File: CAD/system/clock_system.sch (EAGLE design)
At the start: 14 parts

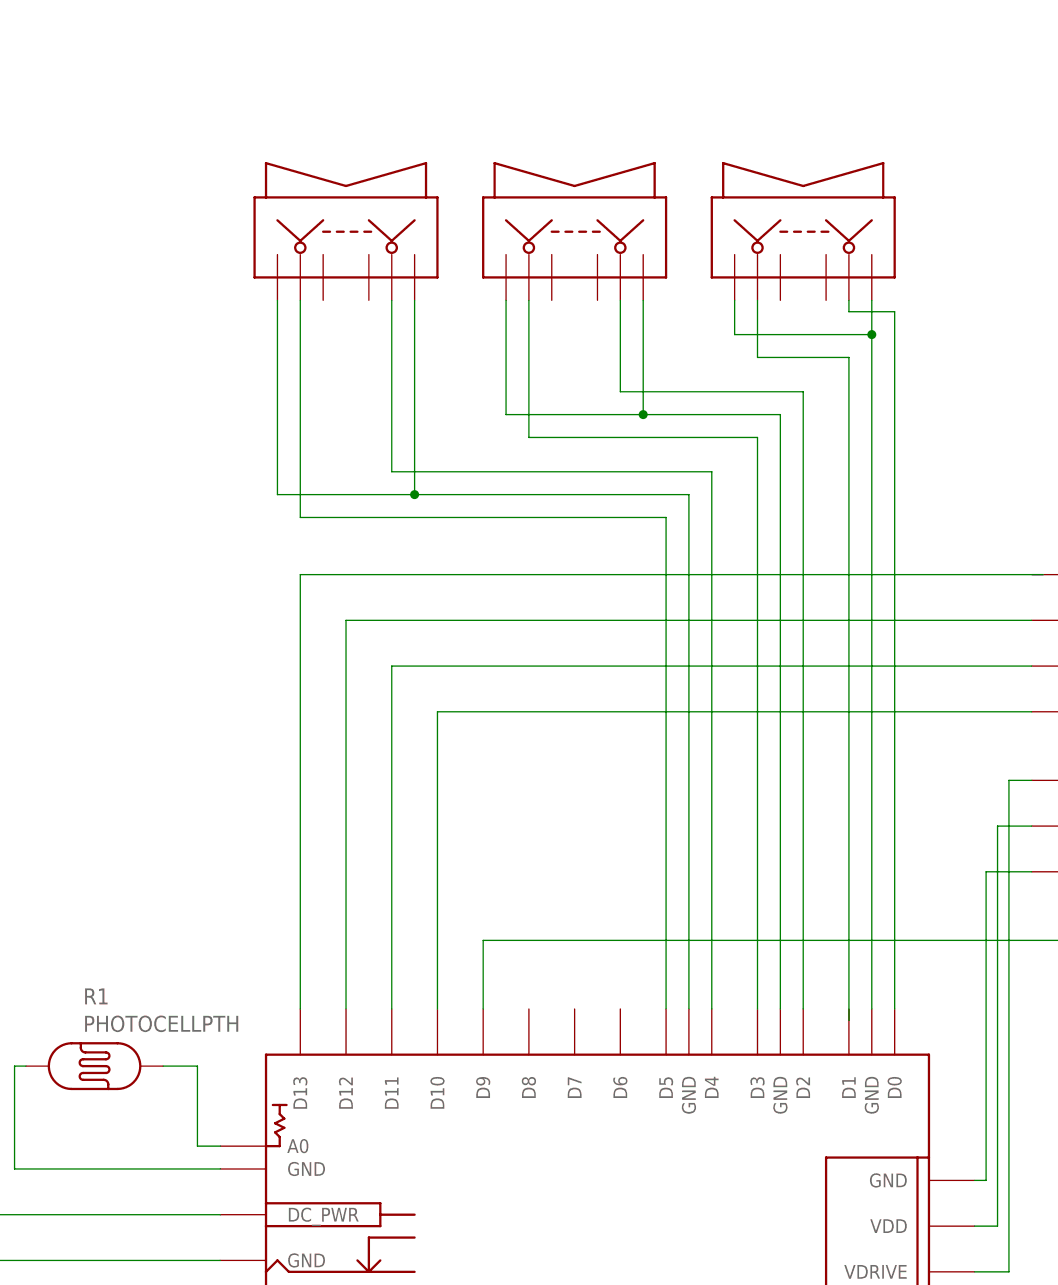
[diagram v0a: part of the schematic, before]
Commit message: Started refactoring code to use new class
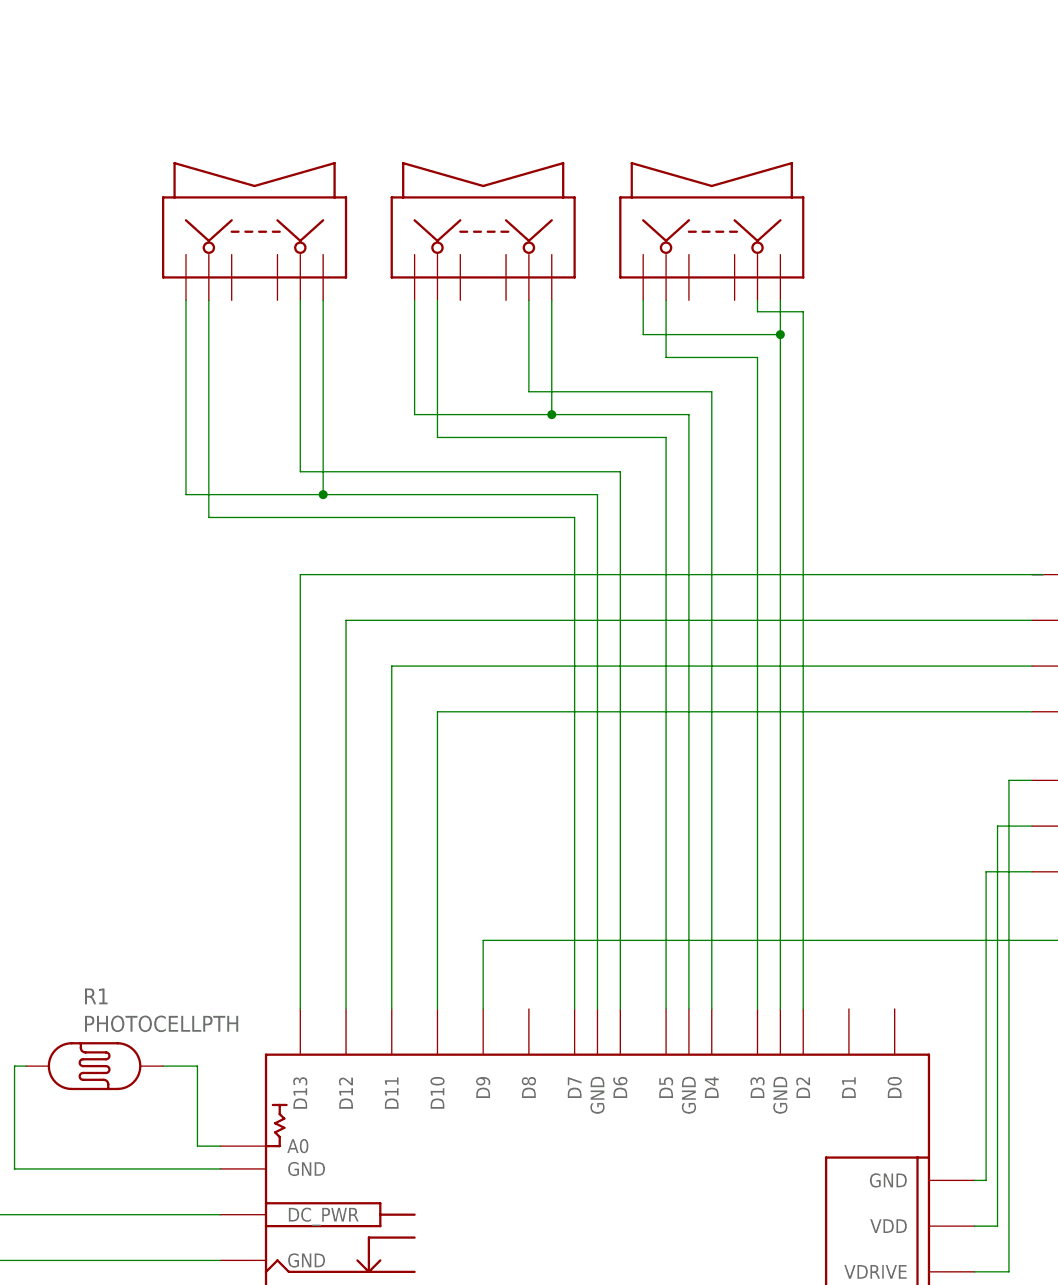
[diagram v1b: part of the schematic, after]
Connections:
- net N$62: now also MOBO.D6; no longer MOBO.D4
- net N$63: now also MOBO.D5; no longer MOBO.D3
- net N$64: now also MOBO.D2; no longer MOBO.D0
- net N$65: now also MOBO.D3
- net N$67: now also MOBO.D4; no longer MOBO.D2
- net N$68: now also MOBO.D7; no longer MOBO.D5
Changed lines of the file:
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@@
 <instance part="MIN2" gate="G$1" x="370.84" y="124.46"/>
 <instance part="COLON" gate="G$1" x="255.27" y="124.46"/>
-<instance part="U$3" gate="G$1" x="81.28" y="124.46" rot="R90"/>
-<instance part="U$1" gate="G$1" x="55.88" y="124.46" rot="R90"/>
-<instance part="U$2" gate="G$1" x="30.48" y="124.46" rot="R90"/>
+<instance part="U$3" gate="G$1" x="71.12" y="124.46" rot="R90"/>
+<instance part="U$1" gate="G$1" x="45.72" y="124.46" rot="R90"/>
+<instance part="U$2" gate="G$1" x="20.32" y="124.46" rot="R90"/>
 <instance part="R1" gate="G$1" x="2.54" y="31.75" smashed="yes">
 <attribute name="NAME" x="1.27" y="38.608" size="1.778" layer="95"/>
@@
 <segment>
 <pinref part="U$1" gate="G$1" pin="P$2"/>
-<wire x1="50.8" y1="116.84" x2="50.8" y2="101.6" width="0.1524" layer="91"/>
-<wire x1="50.8" y1="101.6" x2="76.2" y2="101.6" width="0.1524" layer="91"/>
+<wire x1="40.64" y1="116.84" x2="40.64" y2="101.6" width="0.1524" layer="91"/>
+<wire x1="40.64" y1="101.6" x2="66.04" y2="101.6" width="0.1524" layer="91"/>
+<pinref part="MOBO" gate="G$1" pin="D5"/>
+<wire x1="66.04" y1="38.1" x2="66.04" y2="101.6" width="0.1524" layer="91"/>
+</segment>
+</net>
+<net name="N$66" class="0">
+<segment>
+<pinref part="U$1" gate="G$1" pin="P$1"/>
+<wire x1="38.1" y1="116.84" x2="38.1" y2="104.14" width="0.1524" layer="91"/>
+<pinref part="U$1" gate="G$1" pin="P$6"/>
+<wire x1="38.1" y1="104.14" x2="53.34" y2="104.14" width="0.1524" layer="91"/>
+<wire x1="53.34" y1="104.14" x2="53.34" y2="116.84" width="0.1524" layer="91"/>
+<wire x1="68.58" y1="104.14" x2="53.34" y2="104.14" width="0.1524" layer="91"/>
+<junction x="53.34" y="104.14"/>
+<pinref part="MOBO" gate="G$1" pin="GND@3"/>
+<wire x1="68.58" y1="104.14" x2="68.58" y2="38.1" width="0.1524" layer="91"/>
+</segment>
+</net>
+<net name="N$67" class="0">
+<segment>
+<pinref part="U$1" gate="G$1" pin="P$5"/>
+<wire x1="71.12" y1="106.68" x2="50.8" y2="106.68" width="0.1524" layer="91"/>
+<wire x1="50.8" y1="106.68" x2="50.8" y2="116.84" width="0.1524" layer="91"/>
+<pinref part="MOBO" gate="G$1" pin="D4"/>
+<wire x1="71.12" y1="38.1" x2="71.12" y2="106.68" width="0.1524" layer="91"/>
+</segment>
+</net>
+<net name="N$61" class="0">
+<segment>
+<pinref part="U$3" gate="G$1" pin="P$6"/>
+<wire x1="78.74" y1="116.84" x2="78.74" y2="113.03" width="0.1524" layer="91"/>
+<pinref part="U$3" gate="G$1" pin="P$1"/>
+<wire x1="63.5" y1="116.84" x2="63.5" y2="113.03" width="0.1524" layer="91"/>
+<wire x1="63.5" y1="113.03" x2="78.74" y2="113.03" width="0.1524" layer="91"/>
+<pinref part="MOBO" gate="G$1" pin="GND@2"/>
+<wire x1="78.74" y1="113.03" x2="78.74" y2="38.1" width="0.1524" layer="91"/>
+<junction x="78.74" y="113.03"/>
+</segment>
+</net>
+<net name="N$64" class="0">
+<segment>
+<pinref part="U$3" gate="G$1" pin="P$5"/>
+<wire x1="76.2" y1="116.84" x2="76.2" y2="115.57" width="0.1524" layer="91"/>
+<wire x1="76.2" y1="115.57" x2="81.28" y2="115.57" width="0.1524" layer="91"/>
+<pinref part="MOBO" gate="G$1" pin="D2"/>
+<wire x1="81.28" y1="115.57" x2="81.28" y2="38.1" width="0.1524" layer="91"/>
+</segment>
+</net>
+<net name="N$65" class="0">
+<segment>
+<pinref part="U$3" gate="G$1" pin="P$2"/>
+<wire x1="66.04" y1="116.84" x2="66.04" y2="110.49" width="0.1524" layer="91"/>
+<wire x1="66.04" y1="110.49" x2="76.2" y2="110.49" width="0.1524" layer="91"/>
 <pinref part="MOBO" gate="G$1" pin="D3"/>
-<wire x1="76.2" y1="101.6" x2="76.2" y2="38.1" width="0.1524" layer="91"/>
-</segment>
-</net>
-<net name="N$66" class="0">
-<segment>
-<pinref part="U$1" gate="G$1" pin="P$1"/>
-<wire x1="48.26" y1="116.84" x2="48.26" y2="104.14" width="0.1524" layer="91"/>
-<pinref part="U$1" gate="G$1" pin="P$6"/>
-<wire x1="48.26" y1="104.14" x2="63.5" y2="104.14" width="0.1524" layer="91"/>
-<wire x1="63.5" y1="104.14" x2="63.5" y2="116.84" width="0.1524" layer="91"/>
-<wire x1="78.74" y1="104.14" x2="63.5" y2="104.14" width="0.1524" layer="91"/>
-<junction x="63.5" y="104.14"/>
-<pinref part="MOBO" gate="G$1" pin="GND@3"/>
-<wire x1="78.74" y1="104.14" x2="78.74" y2="38.1" width="0.1524" layer="91"/>
-</segment>
-</net>
-<net name="N$67" class="0">
-<segment>
-<pinref part="U$1" gate="G$1" pin="P$5"/>
-<wire x1="81.28" y1="106.68" x2="60.96" y2="106.68" width="0.1524" layer="91"/>
-<wire x1="60.96" y1="106.68" x2="60.96" y2="116.84" width="0.1524" layer="91"/>
-<pinref part="MOBO" gate="G$1" pin="D2"/>
-<wire x1="81.28" y1="106.68" x2="81.28" y2="38.1" width="0.1524" layer="91"/>
-</segment>
-</net>
-<net name="N$61" class="0">
-<segment>
-<pinref part="U$3" gate="G$1" pin="P$6"/>
-<pinref part="MOBO" gate="G$1" pin="GND@2"/>
-<wire x1="88.9" y1="116.84" x2="88.9" y2="113.03" width="0.1524" layer="91"/>
-<pinref part="U$3" gate="G$1" pin="P$1"/>
-<wire x1="88.9" y1="113.03" x2="88.9" y2="38.1" width="0.1524" layer="91"/>
-<wire x1="73.66" y1="116.84" x2="73.66" y2="113.03" width="0.1524" layer="91"/>
-<wire x1="73.66" y1="113.03" x2="88.9" y2="113.03" width="0.1524" layer="91"/>
-<junction x="88.9" y="113.03"/>
-</segment>
-</net>
-<net name="N$64" class="0">
-<segment>
-<pinref part="U$3" gate="G$1" pin="P$5"/>
-<wire x1="86.36" y1="116.84" x2="86.36" y2="115.57" width="0.1524" layer="91"/>
-<pinref part="MOBO" gate="G$1" pin="D0"/>
-<wire x1="86.36" y1="115.57" x2="91.44" y2="115.57" width="0.1524" layer="91"/>
-<wire x1="91.44" y1="115.57" x2="91.44" y2="38.1" width="0.1524" layer="91"/>
-</segment>
-</net>
-<net name="N$65" class="0">
-<segment>
-<pinref part="U$3" gate="G$1" pin="P$2"/>
-<wire x1="76.2" y1="116.84" x2="76.2" y2="110.49" width="0.1524" layer="91"/>
-<wire x1="76.2" y1="110.49" x2="86.36" y2="110.49" width="0.1524" layer="91"/>
-<wire x1="86.36" y1="110.49" x2="86.36" y2="36.83" width="0.1524" layer="91"/>
+<wire x1="76.2" y1="110.49" x2="76.2" y2="38.1" width="0.1524" layer="91"/>
 </segment>
 </net>
 <net name="N$62" class="0">
 <segment>
-<pinref part="MOBO" gate="G$1" pin="D4"/>
-<wire x1="71.12" y1="38.1" x2="71.12" y2="97.79" width="0.1524" layer="91"/>
-<wire x1="71.12" y1="97.79" x2="35.56" y2="97.79" width="0.1524" layer="91"/>
-<wire x1="35.56" y1="97.79" x2="35.56" y2="116.84" width="0.1524" layer="91"/>
+<wire x1="60.96" y1="97.79" x2="25.4" y2="97.79" width="0.1524" layer="91"/>
+<wire x1="25.4" y1="97.79" x2="25.4" y2="116.84" width="0.1524" layer="91"/>
 <pinref part="U$2" gate="G$1" pin="P$5"/>
+<pinref part="MOBO" gate="G$1" pin="D6"/>
+<wire x1="60.96" y1="97.79" x2="60.96" y2="38.1" width="0.1524" layer="91"/>
 </segment>
 </net>
 <net name="N$68" class="0">
 <segment>
-<pinref part="MOBO" gate="G$1" pin="D5"/>
 <pinref part="U$2" gate="G$1" pin="P$2"/>
-<wire x1="25.4" y1="116.84" x2="25.4" y2="92.71" width="0.1524" layer="91"/>
-<wire x1="25.4" y1="92.71" x2="66.04" y2="92.71" width="0.1524" layer="91"/>
-<wire x1="66.04" y1="92.71" x2="66.04" y2="38.1" width="0.1524" layer="91"/>
+<wire x1="15.24" y1="116.84" x2="15.24" y2="92.71" width="0.1524" layer="91"/>
+<wire x1="15.24" y1="92.71" x2="55.88" y2="92.71" width="0.1524" layer="91"/>
+<pinref part="MOBO" gate="G$1" pin="D7"/>
+<wire x1="55.88" y1="92.71" x2="55.88" y2="38.1" width="0.1524" layer="91"/>
 </segment>
 </net>
@@
 <segment>
 <pinref part="U$2" gate="G$1" pin="P$6"/>
-<wire x1="38.1" y1="95.25" x2="38.1" y2="116.84" width="0.1524" layer="91"/>
-<wire x1="38.1" y1="95.25" x2="68.58" y2="95.25" width="0.1524" layer="91"/>
-<junction x="38.1" y="95.25"/>
+<wire x1="27.94" y1="95.25" x2="27.94" y2="116.84" width="0.1524" layer="91"/>
+<wire x1="27.94" y1="95.25" x2="58.42" y2="95.25" width="0.1524" layer="91"/>
+<junction x="27.94" y="95.25"/>
 <pinref part="U$2" gate="G$1" pin="P$1"/>
-<wire x1="22.86" y1="116.84" x2="22.86" y2="95.25" width="0.1524" layer="91"/>
-<wire x1="22.86" y1="95.25" x2="38.1" y2="95.25" width="0.1524" layer="91"/>
+<wire x1="12.7" y1="116.84" x2="12.7" y2="95.25" width="0.1524" layer="91"/>
+<wire x1="12.7" y1="95.25" x2="27.94" y2="95.25" width="0.1524" layer="91"/>
 <pinref part="MOBO" gate="G$1" pin="GND@4"/>
-<wire x1="68.58" y1="95.25" x2="68.58" y2="38.1" width="0.1524" layer="91"/>
-</segment>
-</net>
+<wire x1="58.42" y1="38.1" x2="58.42" y2="95.25" width="0.1524" layer="91"/>
+</segment>
+</net>
